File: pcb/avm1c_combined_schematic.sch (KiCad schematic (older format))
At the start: 77 parts, among them J1 Video_Output, J10 Front_Conn_1, J11 Front_Conn_3, J12 Back_Conn_2, J13 Back_Conn_3, J14 Back_Conn_1, J15 Front_Conn_4, J16 Back_Conn_4, J17 VIN, J2 Jack_X_CV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

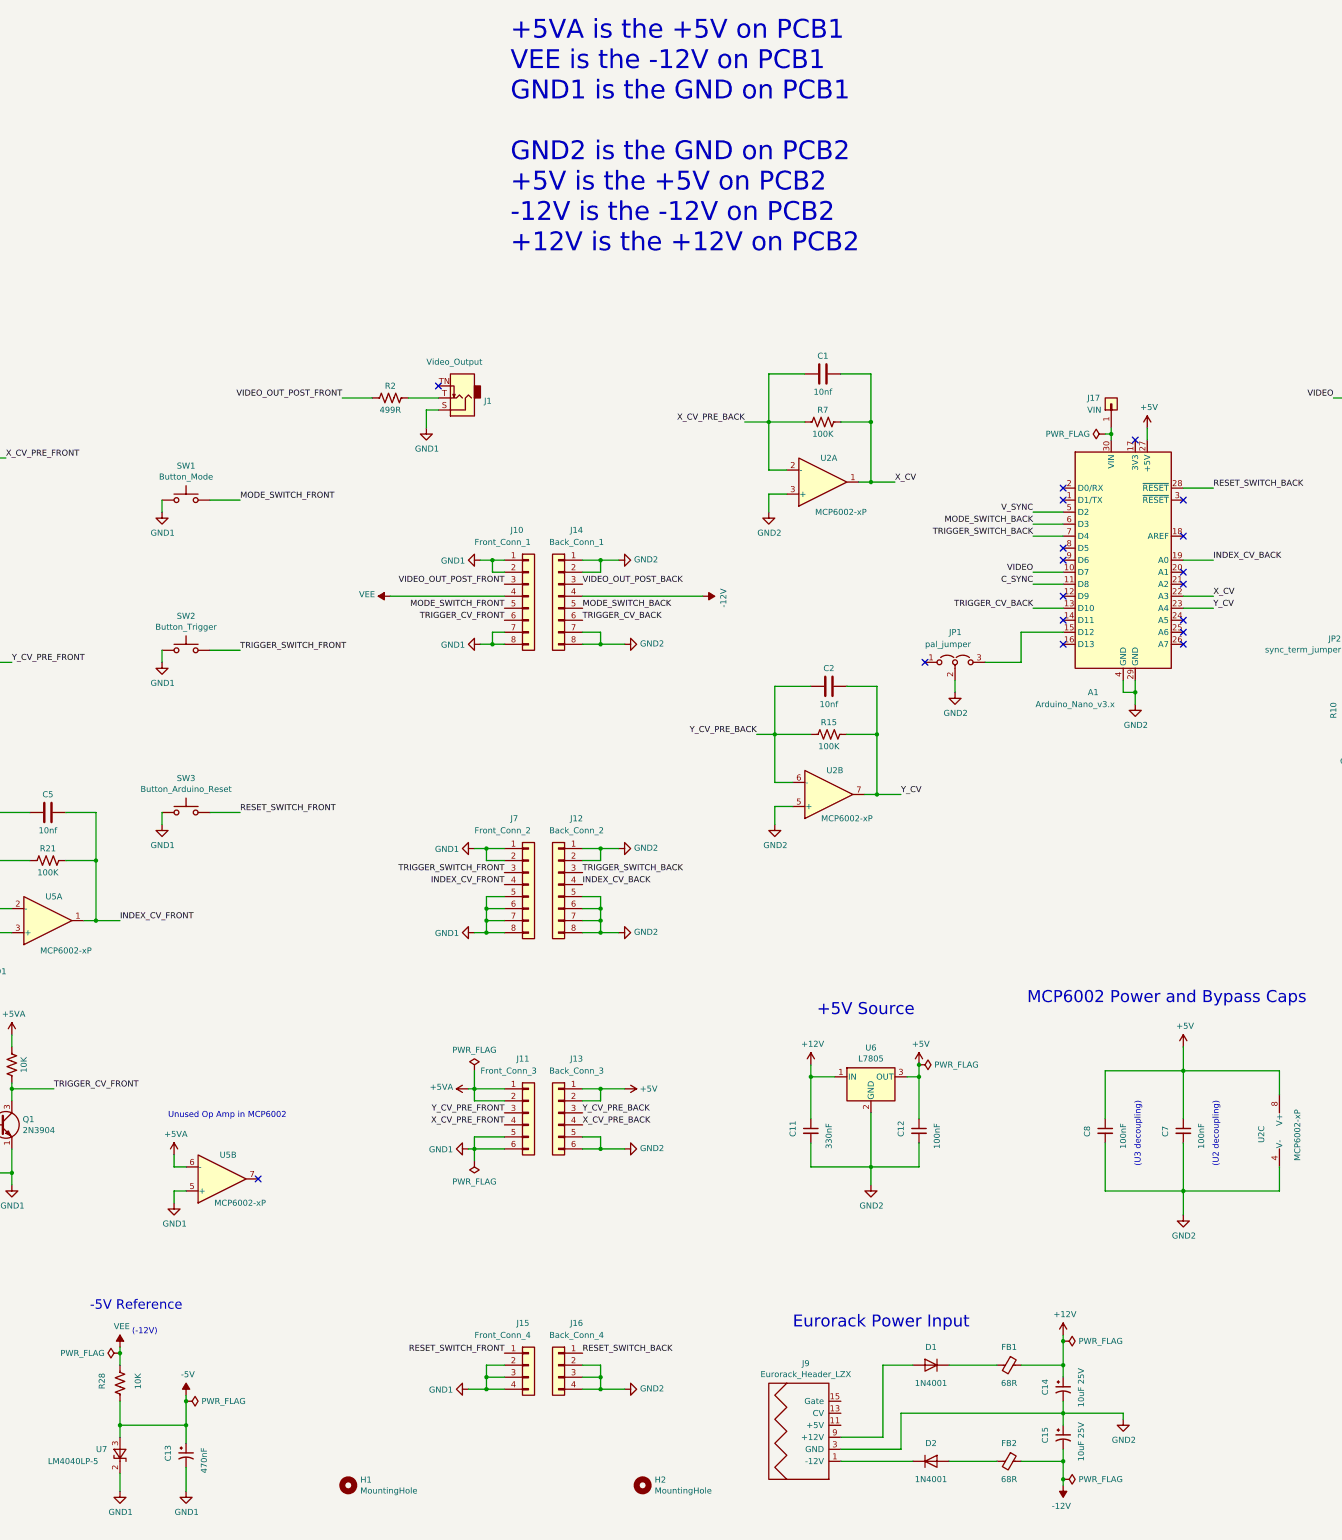
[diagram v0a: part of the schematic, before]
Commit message: update schematic info and export to pdf
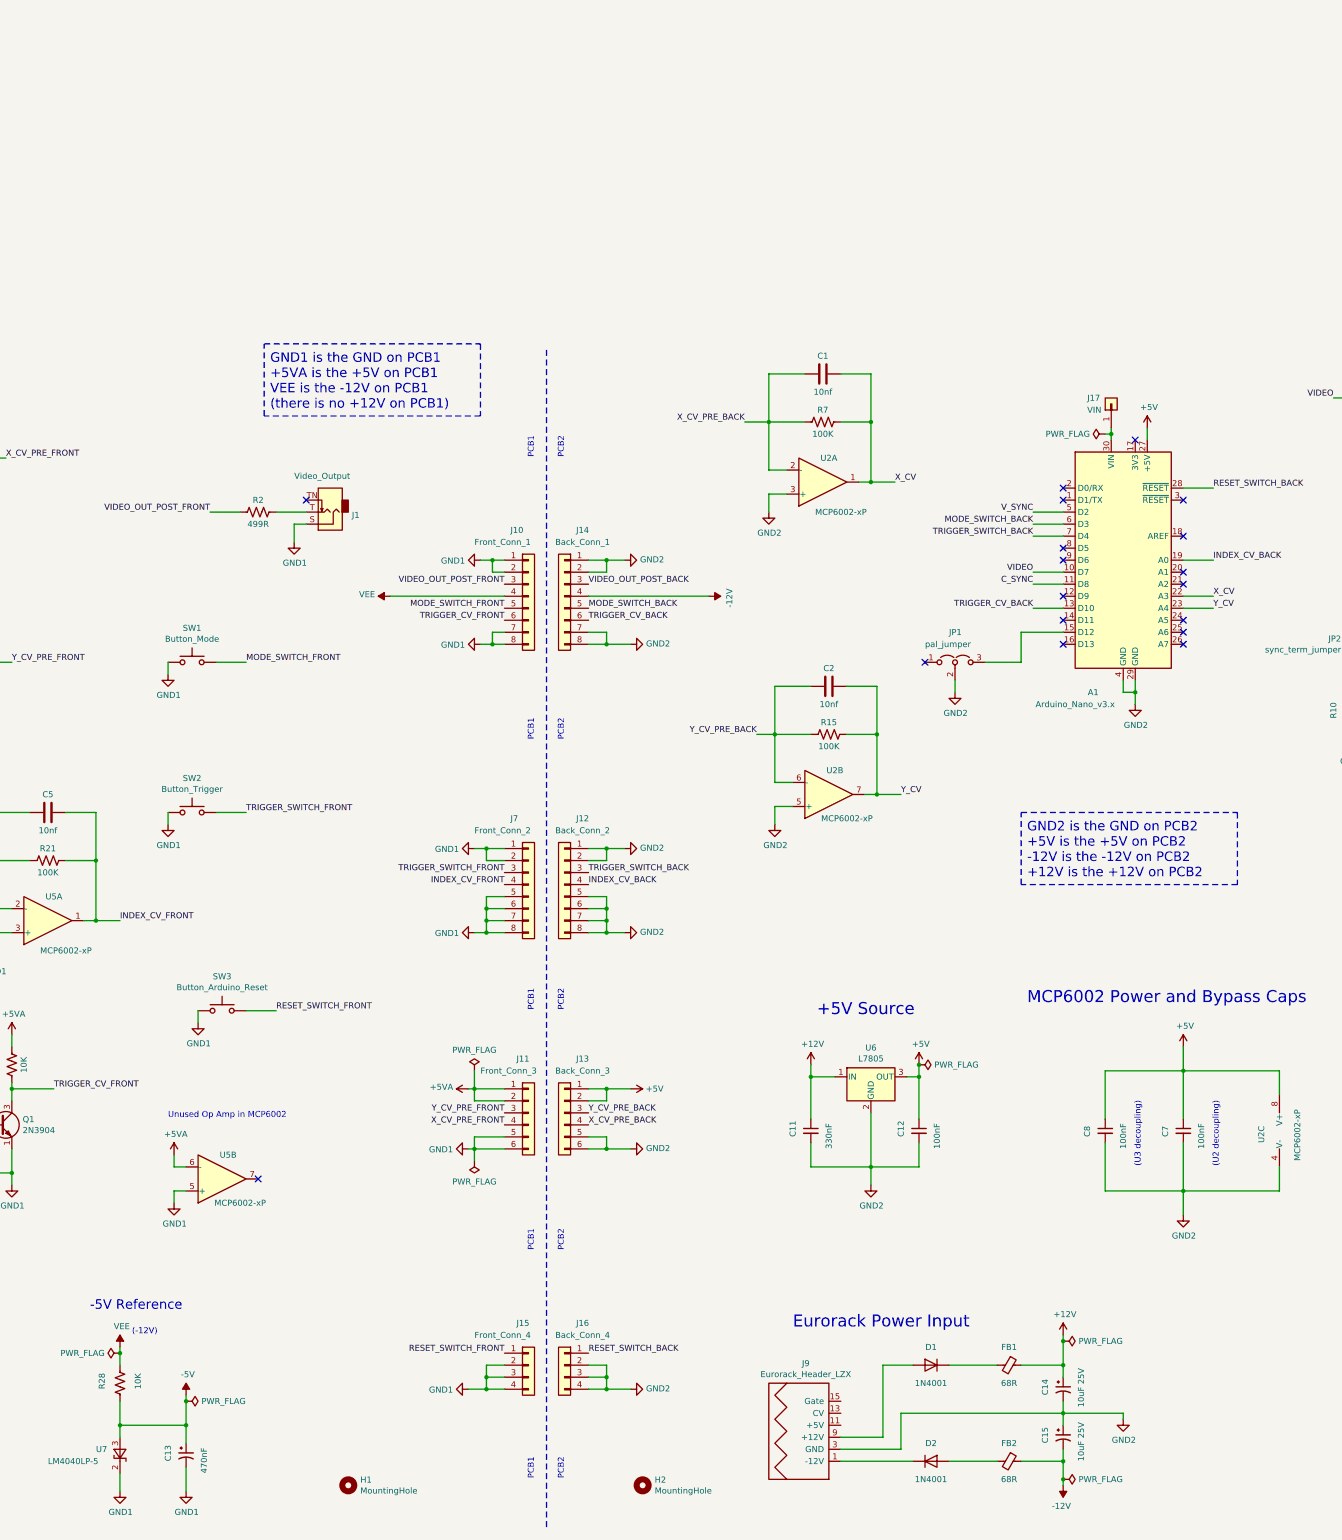
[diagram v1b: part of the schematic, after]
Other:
- note added: "GND1 is the GND on PCB1\n+5VA is the +5V on PCB1\nVEE is the -12V on PCB1\n(there is no +12V on PCB1)"
- note added: "GND2 is the GND on PCB2\n+5V is the +5V on PCB2\n-12V is the -12V on PCB2\n+12V is the +12V on PCB2\n"
- note added: "PCB1"
- note added: "PCB2"
- note removed: "+5VA is the +5V on PCB1\nVEE is the -12V on PCB1\nGND1 is the GND on PCB1\n\nGND2 is the GND on PCB2\n+5V is the +5V on PCB2\n-12V is the -12V on PCB2\n+12V is the +12V on PCB2\n"
- moved on the sheet: J1, J12, J13, J14, J16, R2, SW1, SW2, SW3
